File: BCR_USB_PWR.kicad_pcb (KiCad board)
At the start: 2 copper layers, 21.7 x 13.2 mm, 2 parts, among them CN1 DB9_Female, CN2 UE27AC54100

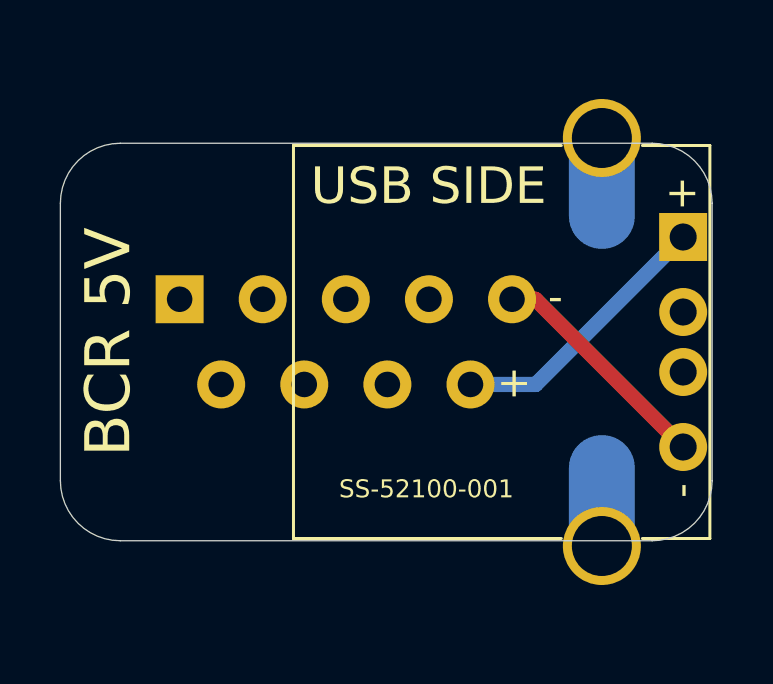
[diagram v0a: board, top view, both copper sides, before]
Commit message: change metal db9 to plastic
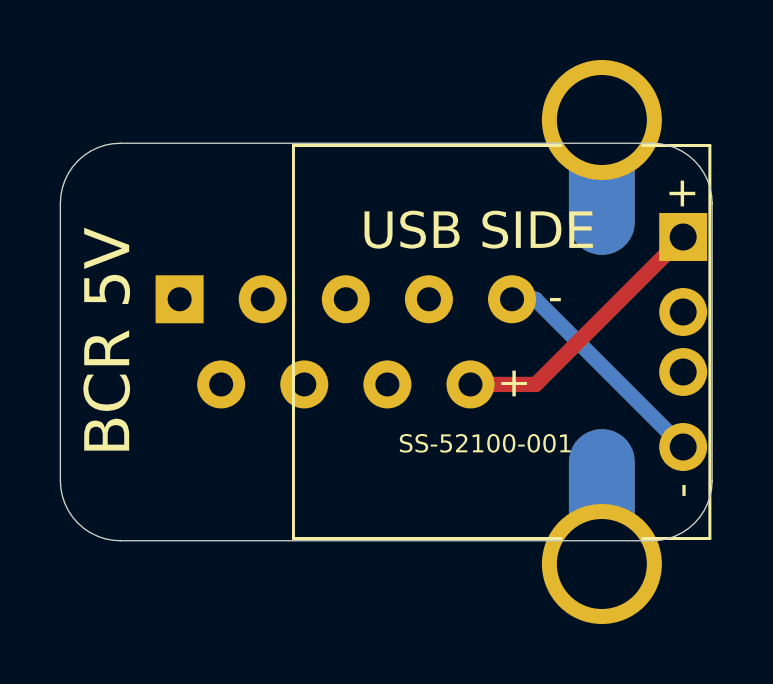
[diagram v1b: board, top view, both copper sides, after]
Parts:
- CN1: footprint 0_LOCAL:DSUB-9_Female_Vertical_metal -> 0_LOCAL:TE-5207826_cut
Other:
- board text added: "TE 5207826"
- board text removed: "A-DF 09 PP/Z"

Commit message: db9 pin 7 is the real GND, not pin 5
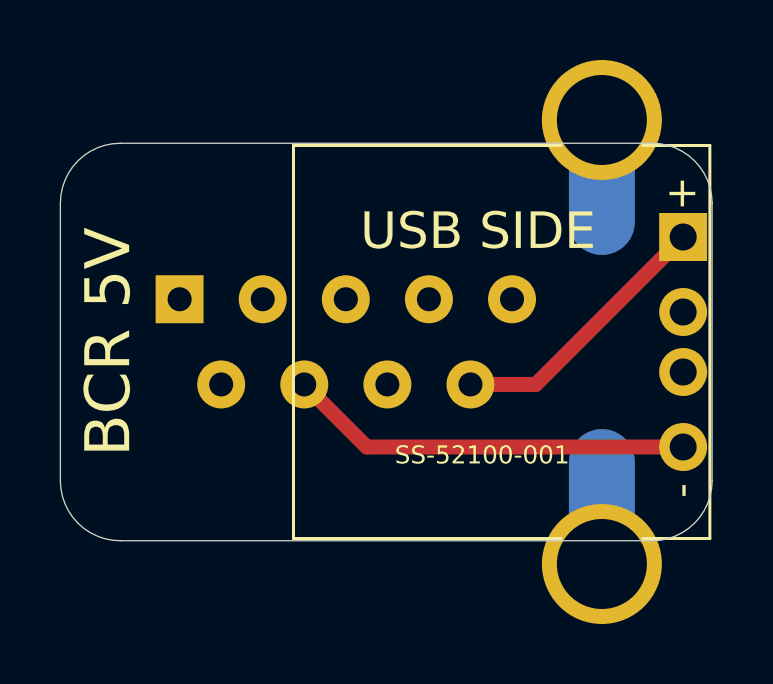
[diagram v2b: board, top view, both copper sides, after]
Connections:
- CN1 pad 5: /GND -> (no net)
- CN1 pad 7: (no net) -> /GND
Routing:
- net /GND: track 7.75 -> 13.5 mm
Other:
- net class Default: clearance 0.2 -> 0.16; trace_width 0.25 -> 0.16; via_dia 0.8 -> 0.42; via_drill 0.4 -> 0.26
- rule trace_clearance: 0.2 -> 0.16
- rule trace_min: 0.2 -> 0.16
- rule via_min_drill: 0.3 -> 0.26
- rule via_min_size: 0.4 -> 0.42
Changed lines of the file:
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@@
-(kicad_pcb (version 20171130) (host pcbnew 5.1.6-c6e7f7d~87~ubuntu19.10.1)
+(kicad_pcb (version 20171130) (host pcbnew 5.1.6-c6e7f7d~87~ubuntu20.04.1)
   (general
     (thickness 1.6)
-    (drawings 29)
+    (drawings 25)
     (tracks 4)
     (zones 0)
@@
   )
   (setup
-    (last_trace_width 0.25)
-    (user_trace_width 0.508)
-    (trace_clearance 0.2)
+    (last_trace_width 0.5)
+    (user_trace_width 0.5)
+    (trace_clearance 0.16)
     (zone_clearance 0.508)
     (zone_45_only no)
-    (trace_min 0.2)
-    (via_size 0.8)
-    (via_drill 0.4)
-    (via_min_size 0.4)
-    (via_min_drill 0.3)
-    (user_via 0.508 0.3048)
+    (trace_min 0.16)
+    (via_size 0.42)
+    (via_drill 0.26)
+    (via_min_size 0.42)
+    (via_min_drill 0.26)
     (uvia_size 0.3)
     (uvia_drill 0.1)
@@
     (mod_text_size 1 1)
     (mod_text_width 0.15)
-    (pad_size 1.524 1.524)
-    (pad_drill 0.762)
+    (pad_size 1.6 1.6)
+    (pad_drill 0.8)
     (pad_to_mask_clearance 0)
     (aux_axis_origin 0 0)
@@
   (net 3 "Net-(CN2-PadSH)")
   (net_class Default "This is the default net class."
-    (clearance 0.2)
-    (trace_width 0.25)
-    (via_dia 0.8)
-    (via_drill 0.4)
+    (clearance 0.16)
+    (trace_width 0.16)
+    (via_dia 0.42)
+    (via_drill 0.26)
     (uvia_dia 0.3)
     (uvia_drill 0.1)
@@
       (effects (font (size 1 1) (thickness 0.15)) (justify mirror))
     )
+    (fp_line (start 2.9 3.91) (end -13.95 3.91) (layer B.CrtYd) (width 0.05))
+    (fp_line (start 2.9 -6.74) (end 2.9 3.91) (layer B.CrtYd) (width 0.05))
+    (fp_line (start -13.95 -6.74) (end 2.9 -6.74) (layer B.CrtYd) (width 0.05))
+    (fp_line (start -13.95 3.91) (end -13.95 -6.74) (layer B.CrtYd) (width 0.05))
+    (fp_line (start -13.40647 0.641744) (end -12.577733 -4.058256) (layer B.SilkS) (width 0.12))
+    (fp_line (start 2.32647 0.641744) (end 1.497733 -4.058256) (layer B.SilkS) (width 0.12))
+    (fp_line (start -10.942952 -5.43) (end -0.137048 -5.43) (layer B.SilkS) (width 0.12))
+    (fp_line (start -11.771689 2.59) (end 0.691689 2.59) (layer B.SilkS) (width 0.12))
+    (fp_line (start -13.358887 0.652163) (end -12.53015 -4.047837) (layer B.Fab) (width 0.1))
+    (fp_line (start 2.278887 0.652163) (end 1.45015 -4.047837) (layer B.Fab) (width 0.1))
+    (fp_line (start -10.954457 -5.37) (end -0.125543 -5.37) (layer B.Fab) (width 0.1))
+    (fp_line (start -11.783194 2.53) (end 0.703194 2.53) (layer B.Fab) (width 0.1))
+    (fp_line (start -5.54 -0.82) (end -5.54 -2.02) (layer Dwgs.User) (width 0.01))
+    (fp_line (start -6.54 -1.42) (end -4.54 -1.42) (layer Dwgs.User) (width 0.01))
     (fp_text user %R (at -5.54 -1.42 180) (layer B.Fab)
       (effects (font (size 1 1) (thickness 0.15)) (justify mirror))
@@
     (fp_arc (start 0.703194 0.93) (end 0.703194 2.53) (angle -100) (layer B.Fab) (width 0.1))
     (fp_arc (start -11.783194 0.93) (end -11.783194 2.53) (angle 100) (layer B.Fab) (width 0.1))
-    (fp_line (start -6.54 -1.42) (end -4.54 -1.42) (layer Dwgs.User) (width 0.01))
-    (fp_line (start -5.54 -0.82) (end -5.54 -2.02) (layer Dwgs.User) (width 0.01))
-    (fp_line (start -11.783194 2.53) (end 0.703194 2.53) (layer B.Fab) (width 0.1))
-    (fp_line (start -10.954457 -5.37) (end -0.125543 -5.37) (layer B.Fab) (width 0.1))
-    (fp_line (start 2.278887 0.652163) (end 1.45015 -4.047837) (layer B.Fab) (width 0.1))
-    (fp_line (start -13.358887 0.652163) (end -12.53015 -4.047837) (layer B.Fab) (width 0.1))
-    (fp_line (start -11.771689 2.59) (end 0.691689 2.59) (layer B.SilkS) (width 0.12))
-    (fp_line (start -10.942952 -5.43) (end -0.137048 -5.43) (layer B.SilkS) (width 0.12))
-    (fp_line (start 2.32647 0.641744) (end 1.497733 -4.058256) (layer B.SilkS) (width 0.12))
-    (fp_line (start -13.40647 0.641744) (end -12.577733 -4.058256) (layer B.SilkS) (width 0.12))
-    (fp_line (start -13.95 3.91) (end -13.95 -6.74) (layer B.CrtYd) (width 0.05))
-    (fp_line (start -13.95 -6.74) (end 2.9 -6.74) (layer B.CrtYd) (width 0.05))
-    (fp_line (start 2.9 -6.74) (end 2.9 3.91) (layer B.CrtYd) (width 0.05))
-    (fp_line (start 2.9 3.91) (end -13.95 3.91) (layer B.CrtYd) (width 0.05))
     (pad 9 thru_hole circle (at -9.695 -2.84 180) (size 1.6 1.6) (drill 0.8) (layers *.Cu *.Mask)
       (net 1 /+5V))
     (pad 8 thru_hole circle (at -6.925 -2.84 180) (size 1.6 1.6) (drill 0.8) (layers *.Cu *.Mask))
-    (pad 7 thru_hole circle (at -4.155 -2.84 180) (size 1.6 1.6) (drill 0.8) (layers *.Cu *.Mask))
+    (pad 7 thru_hole circle (at -4.155 -2.84 180) (size 1.6 1.6) (drill 0.8) (layers *.Cu *.Mask)
+      (net 2 /GND))
     (pad 6 thru_hole circle (at -1.385 -2.84 180) (size 1.6 1.6) (drill 0.8) (layers *.Cu *.Mask))
-    (pad 5 thru_hole circle (at -11.08 0 180) (size 1.6 1.6) (drill 0.8) (layers *.Cu *.Mask)
-      (net 2 /GND))
+    (pad 5 thru_hole circle (at -11.08 0 180) (size 1.6 1.6) (drill 0.8) (layers *.Cu *.Mask))
     (pad 4 thru_hole circle (at -8.31 0 180) (size 1.6 1.6) (drill 0.8) (layers *.Cu *.Mask))
     (pad 3 thru_hole circle (at -5.54 0 180) (size 1.6 1.6) (drill 0.8) (layers *.Cu *.Mask))
@@
       (effects (font (size 1 1) (thickness 0.15)))
     )
+    (fp_line (start -6.75 10.375) (end 6.75 10.375) (layer F.CrtYd) (width 0.05))
+    (fp_line (start -6.75 -3.94) (end -6.75 10.375) (layer F.CrtYd) (width 0.05))
+    (fp_line (start 6.75 -3.94) (end 6.75 10.375) (layer F.CrtYd) (width 0.05))
+    (fp_line (start -6.75 -3.94) (end 6.75 -3.94) (layer F.CrtYd) (width 0.05))
+    (fp_line (start 6.55 10.28) (end -6.55 10.28) (layer F.SilkS) (width 0.1))
+    (fp_line (start 6.55 -3.6) (end 6.55 -1.35) (layer F.SilkS) (width 0.1))
+    (fp_line (start -6.55 10.28) (end 6.55 10.28) (layer F.Fab) (width 0.1))
+    (fp_line (start -6.55 -3.6) (end -6.55 10.28) (layer F.Fab) (width 0.1))
+    (fp_line (start 6.55 -3.6) (end 6.55 10.28) (layer F.Fab) (width 0.1))
+    (fp_line (start -6.55 -3.6) (end 6.55 -3.6) (layer F.Fab) (width 0.1))
+    (fp_line (start -6.55 -3.6) (end -6.55 -1.35) (layer F.SilkS) (width 0.1))
+    (fp_line (start -6.55 1.35) (end -6.55 10.28) (layer F.SilkS) (width 0.1))
+    (fp_line (start 6.55 1.35) (end 6.55 10.28) (layer F.SilkS) (width 0.1))
+    (fp_line (start -6.55 -3.6) (end 6.55 -3.6) (layer F.SilkS) (width 0.1))
     (fp_text user %R (at -0.025 0.975 270) (layer F.Fab)
       (effects (font (size 1 1) (thickness 0.15)))
     )
-    (fp_line (start -6.55 -3.6) (end 6.55 -3.6) (layer F.SilkS) (width 0.1))
-    (fp_line (start 6.55 1.35) (end 6.55 10.28) (layer F.SilkS) (width 0.1))
-    (fp_line (start -6.55 1.35) (end -6.55 10.28) (layer F.SilkS) (width 0.1))
-    (fp_line (start -6.55 -3.6) (end -6.55 -1.35) (layer F.SilkS) (width 0.1))
-    (fp_line (start -6.55 -3.6) (end 6.55 -3.6) (layer F.Fab) (width 0.1))
-    (fp_line (start 6.55 -3.6) (end 6.55 10.28) (layer F.Fab) (width 0.1))
-    (fp_line (start -6.55 -3.6) (end -6.55 10.28) (layer F.Fab) (width 0.1))
-    (fp_line (start -6.55 10.28) (end 6.55 10.28) (layer F.Fab) (width 0.1))
-    (fp_line (start 6.55 -3.6) (end 6.55 -1.35) (layer F.SilkS) (width 0.1))
-    (fp_line (start 6.55 10.28) (end -6.55 10.28) (layer F.SilkS) (width 0.1))
-    (fp_line (start -6.75 -3.94) (end 6.75 -3.94) (layer F.CrtYd) (width 0.05))
-    (fp_line (start 6.75 -3.94) (end 6.75 10.375) (layer F.CrtYd) (width 0.05))
-    (fp_line (start -6.75 -3.94) (end -6.75 10.375) (layer F.CrtYd) (width 0.05))
-    (fp_line (start -6.75 10.375) (end 6.75 10.375) (layer F.CrtYd) (width 0.05))
     (pad SH smd oval (at 6.8 0 270) (size 4.8 2.2) (drill (offset -1.5 0)) (layers B.Cu B.Paste B.Mask)
       (net 3 "Net-(CN2-PadSH)"))
@@
   (gr_arc (start 119.5 91.133) (end 119.5 89.133) (angle -90) (layer Edge.Cuts) (width 0.025))
   (gr_arc (start 119.5 100.383) (end 117.5 100.383) (angle -90) (layer Edge.Cuts) (width 0.025))
-  (gr_text + (at 132.625 97.108) (layer B.SilkS)
-    (effects (font (size 1 1) (thickness 0.15)) (justify mirror))
-  )
-  (gr_text - (at 134 94.258) (layer B.SilkS)
-    (effects (font (size 1 1) (thickness 0.15)) (justify mirror))
-  )
-  (gr_text - (at 134 94.258) (layer F.SilkS)
-    (effects (font (size 1 1) (thickness 0.15)))
-  )
-  (gr_text + (at 132.625 97.108) (layer F.SilkS)
-    (effects (font (size 1 1) (thickness 0.15)))
-  )
   (gr_text - (at 138.2 100.708 90) (layer F.SilkS)
     (effects (font (size 1 1) (thickness 0.15)))
@@
     (effects (font (size 0.8 0.8) (thickness 0.1)) (justify mirror))
   )
-  (gr_text SS-52100-001 (at 131.675 99.158) (layer F.SilkS)
+  (gr_text SS-52100-001 (at 131.56 99.528) (layer F.SilkS)
     (effects (font (size 0.6 0.6) (thickness 0.1)))
   )
@@
     (effects (font (size 1.2192 1.2192) (thickness 0.2032)))
   )
-  (segment (start 133.345 97.173) (end 131.17 97.173) (width 0.508) (layer F.Cu) (net 1))
-  (segment (start 138.26 92.258) (end 133.345 97.173) (width 0.508) (layer F.Cu) (net 1))
-  (segment (start 133.335 94.333) (end 132.555 94.333) (width 0.508) (layer B.Cu) (net 2))
-  (segment (start 138.26 99.258) (end 133.335 94.333) (width 0.508) (layer B.Cu) (net 2))
+  (segment (start 133.345 97.173) (end 131.17 97.173) (width 0.5) (layer F.Cu) (net 1))
+  (segment (start 138.26 92.258) (end 133.345 97.173) (width 0.5) (layer F.Cu) (net 1))
+  (segment (start 127.715 99.258) (end 138.26 99.258) (width 0.5) (layer F.Cu) (net 2))
+  (segment (start 125.63 97.173) (end 127.715 99.258) (width 0.5) (layer F.Cu) (net 2))
 )
